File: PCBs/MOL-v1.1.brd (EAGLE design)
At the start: 165.1 x 81 mm, 67 parts, among them IC1 ULN2803, IC2 ULN2803, J1 SERVO 1, J2 SERVO 2, U1 SN74LVC2G04DBV, U2 JOYSTICKPTH, U3 JOYSTICKPTH

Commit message: signal name changes in MOL PCB v1.1
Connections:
- removed net A1: J3.2, TM1.2
- removed net A10: J8.2, TM10.2
- removed net A11: TM11.2
- removed net A12: TM12.2
- removed net A2: J4.2, TM2.2
- removed net A3: TM3.2
- removed net A4: TM4.2
- removed net A5: J5.2, TM5.2
- removed net A6: J6.2, TM6.2
- removed net A7: TM7.2
- removed net A8: TM8.2
- removed net A9: J7.2, TM9.2
- net AN1: now also J3.2, TM1.2
- net AN10: now also J8.2, TM10.2
- net AN11: now also TM11.2
- net AN12: now also TM12.2
- net AN2: now also J4.2, TM2.2
- net AN3: now also TM3.2
- net AN4: now also TM4.2
- net AN5: now also J5.2, TM5.2
- net AN6: now also J6.2, TM6.2
- net AN7: now also TM7.2
- net AN8: now also TM8.2
- net AN9: now also J7.2, TM9.2
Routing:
- net A10: track 152.7 -> 0.00 mm, vias 1 -> 0
- net AN10: track 0.00 -> 152.6 mm, vias 0 -> 1
- net A9: track 149.9 -> 0.00 mm, vias 2 -> 0
- net AN9: track 0.00 -> 149.9 mm, vias 0 -> 2
- net AN12: track 0.00 -> 140.8 mm, vias 0 -> 4
- net A12: track 140.8 -> 0.00 mm, vias 4 -> 0
- net AN11: track 0.00 -> 131.3 mm, vias 0 -> 3
- net A11: track 131.3 -> 0.00 mm, vias 3 -> 0
- net A6: track 117.4 -> 0.00 mm, vias 2 -> 0
- net AN6: track 0.00 -> 117.3 mm, vias 0 -> 2
- net A2: track 94.4 -> 0.00 mm, vias 1 -> 0
- net AN2: track 0.00 -> 94.3 mm, vias 0 -> 1
- net AN8: track 0.00 -> 84.4 mm, vias 0 -> 3
- net A8: track 84.4 -> 0.00 mm, vias 3 -> 0
- net A1: track 81.9 -> 0.00 mm
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
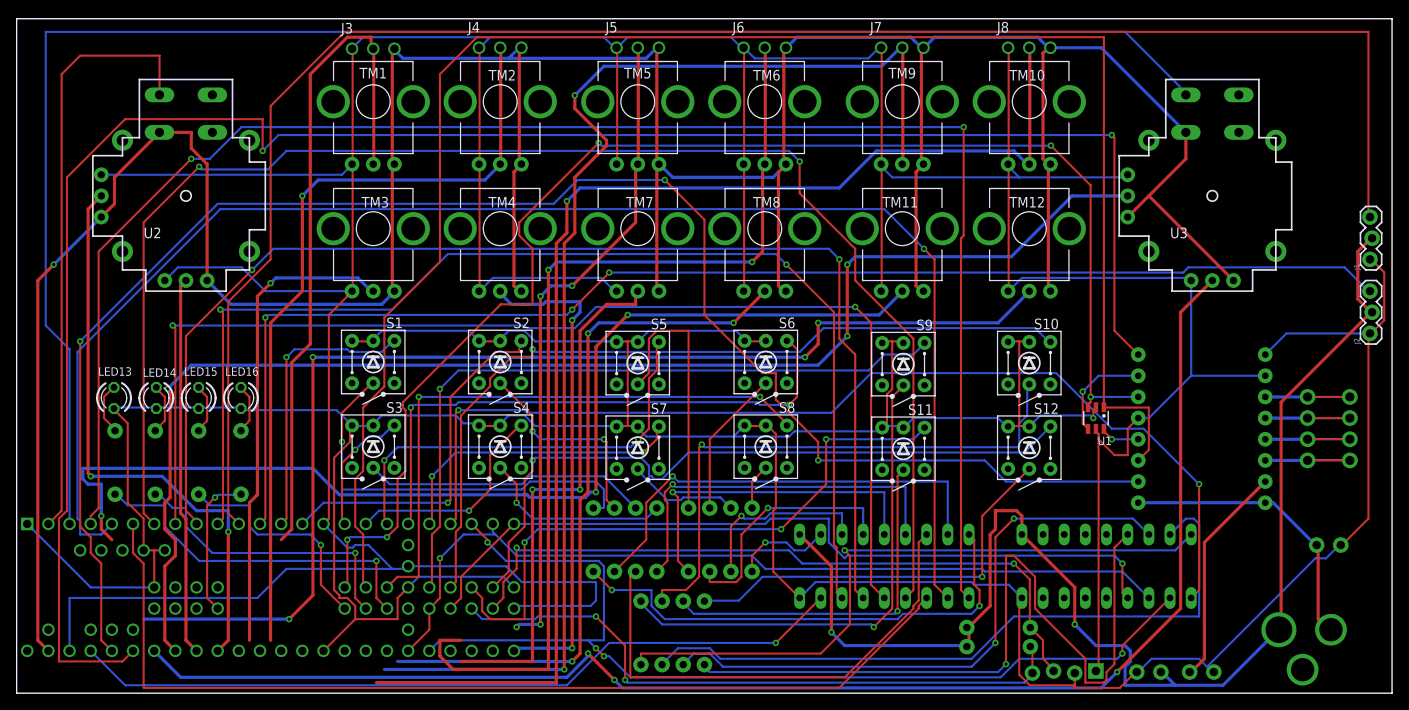
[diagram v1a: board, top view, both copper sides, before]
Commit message: Processor working, refactored Arduino code
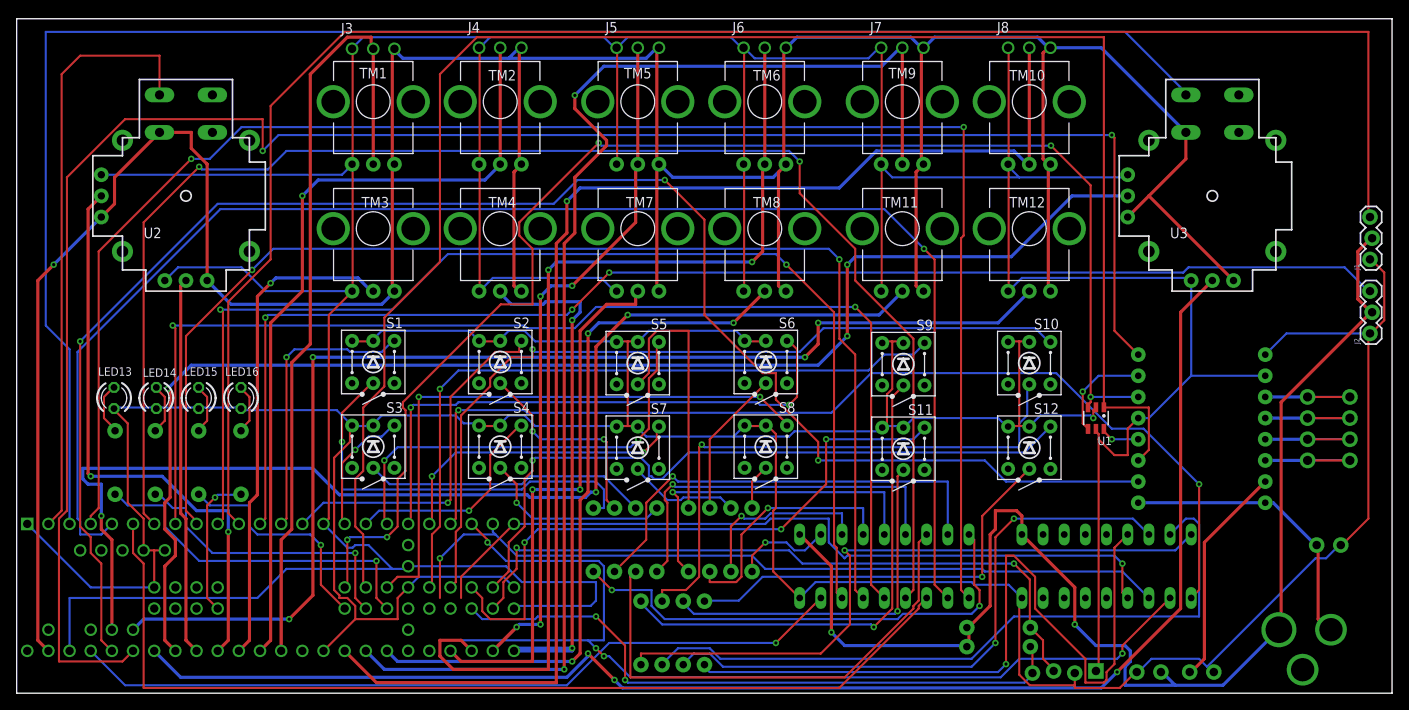
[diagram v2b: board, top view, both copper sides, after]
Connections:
- net B1 renamed BTN1
- net B10 renamed BTN10
- net B11 renamed BTN11
- net B12 renamed BTN12
- net B2 renamed BTN2
- net B3 renamed BTN3
- net B4 renamed BTN4
- net B5 renamed BTN5
- net B6 renamed BTN6
- net B7 renamed BTN7
- net B8 renamed BTN8
- net B9 renamed BTN9
- net M_AIN renamed M_A_IN
- net M_BIN renamed M_B_IN
- net M_JOYB renamed JOY_BTN_M
- net M_JOYH renamed JOY_AN_H_M
- net M_JOYV renamed JOY_AN_V_M
- net M_PWMA renamed M_PWM_A
- net M_PWMB renamed M_PWM_B
- net S_JOYB renamed JOY_BTN_S
- net S_JOYH renamed JOY_AN_H_S
- net S_JOYV renamed JOY_AN_V_S
- net L10: no longer TEENSY.37
- net L11: no longer TEENSY.38, TEENSY.50
- net L12: no longer TEENSY.49
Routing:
- net AN1: track 81.9 -> 95.4 mm
- net AN11: track 131.3 -> 142.1 mm
- net L11: track 103.5 -> 95.6 mm
- net AN4: track 59.2 -> 66.5 mm
- net AN10: track 152.6 -> 158.0 mm
- net AN5: track 78.6 -> 82.6 mm
- net AN9: track 149.9 -> 153.0 mm
- net AN6: track 117.3 -> 119.2 mm
- net AN2: track 94.3 -> 96.2 mm
- net AN12: track 140.8 -> 142.6 mm
- net AN7: track 63.6 -> 65.4 mm
- net AN3: track 57.2 -> 59.0 mm
- net L12: track 95.2 -> 93.4 mm
- net L10: track 124.7 -> 122.9 mm
- net AN8: track 84.4 -> 86.2 mm
